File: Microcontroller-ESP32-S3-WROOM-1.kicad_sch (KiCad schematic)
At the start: 17 parts, among them U1 ESP32-S3-WROOM-1, U4 CP2102N-Axx-xQFN20

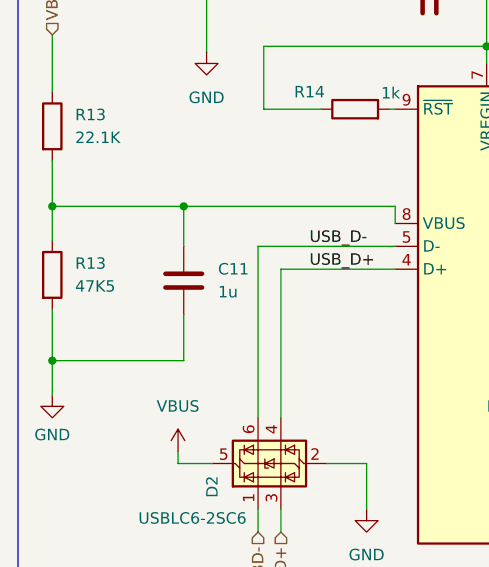
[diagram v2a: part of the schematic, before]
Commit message: refactor(schematic): update resistor footprints and component metadata
Change resistor footprints from 0805 to 0201 metric and populate detailed component properties including manufacturer, part numbers, datasheets, and distributor links for improved BOM accuracy.
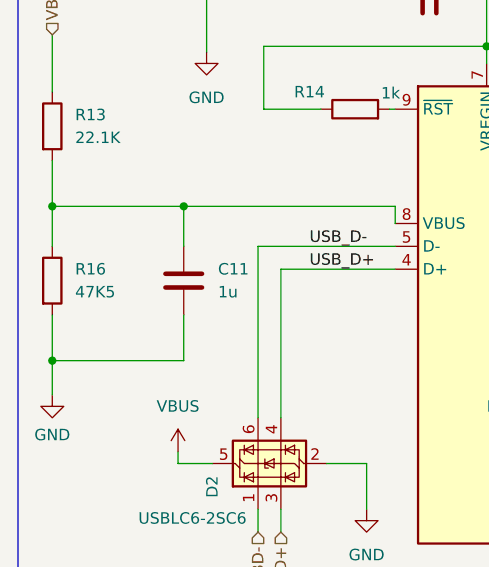
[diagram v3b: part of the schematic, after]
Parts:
- removed R13: 47K5, Resistor_SMD:R_0805_2012Metric, symbol Device:R
- added R16: 47K5, Resistor_SMD:R_0201_0603Metric, symbol Device:R
- R13: footprint Resistor_SMD:R_0805_2012Metric -> Resistor_SMD:R_0201_0603Metric; Distributor_link_1 (none) -> https://eu.mouser.com/ProductDetail/Susumu/RG0603Q-2212-D-T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; Distributor_link_2 (none) -> https://www.digikey.com/en/products/detail/susumu/RG0603Q-2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; LCSC (none) -> https://www.lcsc.com/search?q=VES4R7M1VTR-0405&s_z=n_q_VES4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; Manufacturer (none) -> Susumu; Manufacturer_part_number (none) -> RG0603Q-2212-D-T10
- R14: footprint Resistor_SMD:R_0805_2012Metric -> Resistor_SMD:R_0201_0603Metric; Distributor_link_1 (none) -> https://eu.mouser.com/ProductDetail/Susumu/RG0603P-102-B-T1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; Distributor_link_2 (none) -> https://www.digikey.com/en/products/detail/susumu/RG0603P-1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; LCSC (none) -> C20135023; Manufacturer (none) -> Susumu; Manufacturer_part_number (none) -> RG0603P-102-B-T10
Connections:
- net GND: now also R16.2
- net at C11.1, R13.2, U4.8 (VBUS): now also R16.1
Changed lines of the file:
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@@
-	(wire
-		(pts
-			(xy 19.05 153.035) (xy 19.05 158.75)
-		)
-		(stroke
-			(width 0)
-			(type default)
-		)
-	)
 	(wire
 		(pts
@@
 	(wire
 		(pts
+			(xy 19.05 141.605) (xy 19.05 146.05)
+		)
+		(stroke
+			(width 0)
+			(type default)
+		)
+	)
+	(wire
+		(pts
 			(xy 57.15 141.605) (xy 57.15 143.51)
 		)
@@
 	(wire
 		(pts
+			(xy 19.05 153.67) (xy 19.05 158.75)
+		)
+		(stroke
+			(width 0)
+			(type default)
+		)
+	)
+	(wire
+		(pts
 			(xy 82.55 168.91) (xy 86.36 168.91)
 		)
@@
 		(pts
 			(xy 44.45 165.1) (xy 44.45 148.59)
-		)
-		(stroke
-			(width 0)
-			(type default)
-		)
-	)
-	(wire
-		(pts
-			(xy 19.05 141.605) (xy 19.05 145.415)
 		)
 		(stroke
@@
 			)
 		)
-		(property "Footprint" "Resistor_SMD:R_0805_2012Metric"
+		(property "Footprint" "Resistor_SMD:R_0201_0603Metric"
 			(at 17.272 132.715 90)
 			(effects
@@
 			)
 		)
-		(property "Datasheet" "~"
+		(property "Datasheet" "https://eu.mouser.com/datasheet/3/826/1/n_catalog_partition01_en.pdf"
 			(at 19.05 132.715 0)
 			(effects
@@
 			)
 		)
-		(property "Description" "Resistor"
+		(property "Description" "Thin Film Resistors - SMD Thin Film Chip Resistors 0201 size, 0.063W, 22.1K ohm, 0.5%, 50ppm AEC Q200 Qualified Anti-sulfur"
+			(at 19.05 132.715 0)
+			(effects
+				(font
+					(size 1.27 1.27)
+				)
+				(hide yes)
+			)
+		)
+		(property "Manufacturer" "Susumu"
+			(at 19.05 132.715 0)
+			(effects
+				(font
+					(size 1.27 1.27)
+				)
+				(hide yes)
+			)
+		)
+		(property "Manufacturer_part_number" "RG0603Q-2212-D-T10"
+			(at 19.05 132.715 0)
+			(effects
+				(font
+					(size 1.27 1.27)
+				)
+				(hide yes)
+			)
+		)
+		(property "Distributor_link_1" "https://eu.mouser.com/ProductDetail/Susumu/RG0603Q-2212-D-T10?qs=amGC7iS6iy8tfDEqHW4FPw%3D%3D"
+			(at 19.05 132.715 0)
+			(effects
+				(font
+					(size 1.27 1.27)
+				)
+				(hide yes)
+			)
+		)
+		(property "Distributor_link_2" "https://www.digikey.com/en/products/detail/susumu/RG0603Q-2212-D-T10/18103229?s=N4IgTCBcDaIEoHEAMA2JBmAigWjGAjGNgCLYAq%2BSIAugL5A"
+			(at 19.05 132.715 0)
+			(effects
+				(font
+					(size 1.27 1.27)
+				)
+				(hide yes)
+			)
+		)
+		(property "LCSC" "https://www.lcsc.com/search?q=VES4R7M1VTR-0405&s_z=n_q_VES4R7M1VTR-0405"
 			(at 19.05 132.715 0)
 			(effects
@@
 			)
 		)
-		(property "Footprint" "Resistor_SMD:R_0805_2012Metric"
+		(property "Footprint" "Resistor_SMD:R_0201_0603Metric"
 			(at 52.705 132.588 90)
 			(effects
@@
 			)
 		)
-		(property "Datasheet" "~"
+		(property "Datasheet" "https://eu.mouser.com/datasheet/3/826/1/n_catalog_partition01_en.pdf"
 			(at 52.705 130.81 0)
 			(effects
@@
 			)
 		)
-		(property "Description" "Resistor"
+		(property "Description" "Thin Film Resistors - SMD Thin Film Chip Resistors 0201 size, 0.063W, 1K ohm, 0.1%, 25ppm AEC Q200 Qualified Anti-sulfur"
 			(at 52.705 130.81 0)
+			(effects
+				(font
+					(size 1.27 1.27)
+				)
+				(hide yes)
+			)
+		)
+		(property "Manufacturer" "Susumu"
+			(at 52.705 130.81 90)
+			(effects
+				(font
+					(size 1.27 1.27)
+				)
+				(hide yes)
+			)
+		)
+		(property "Manufacturer_part_number" "RG0603P-102-B-T10"
+			(at 52.705 130.81 90)
+			(effects
+				(font
+					(size 1.27 1.27)
+				)
+				(hide yes)
+			)
+		)
+		(property "Distributor_link_1" "https://eu.mouser.com/ProductDetail/Susumu/RG0603P-102-B-T10?qs=amGC7iS6iy%2F0QPamw0jmkg%3D%3D"
+			(at 52.705 130.81 90)
+			(effects
+				(font
+					(size 1.27 1.27)
+				)
+				(hide yes)
+			)
+		)
+		(property "Distributor_link_2" "https://www.digikey.com/en/products/detail/susumu/RG0603P-102-B-T10/18103206?s=N4IgTCBcDaIEoHEAMA2JBmACgWgIxLGwCFsAVfEAXQF8g"
+			(at 52.705 130.81 90)
+			(effects
+				(font
+					(size 1.27 1.27)
+				)
+				(hide yes)
+			)
+		)
+		(property "LCSC" "C20135023"
+			(at 52.705 130.81 90)
 			(effects
 				(font
@@
 	)
 	(symbol
+		(lib_id "Device:R")
+		(at 19.05 149.86 0)
+		(unit 1)
+		(exclude_from_sim no)
+		(in_bom yes)
+		(on_board yes)
+		(dnp no)
+		(fields_autoplaced yes)
+		(property "Reference" "R16"
+			(at 21.59 148.5899 0)
+			(effects
+				(font
+					(size 1.27 1.27)
+				)
+				(justify left)
+			)
+		)
+		(property "Value" "47K5"
+			(at 21.59 151.1299 0)
+			(effects
+				(font
+					(size 1.27 1.27)
+				)
+				(justify left)
+			)
+		)
+		(property "Footprint" "Resistor_SMD:R_0201_0603Metric"
+			(at 17.272 149.86 90)
+			(effects
+				(font
+					(size 1.27 1.27)
+				)
+				(hide yes)
+			)
+		)
+		(property "Datasheet" "https://eu.mouser.com/datasheet/3/826/1/n_catalog_partition01_en.pdf"
+			(at 19.05 149.86 0)
+			(effects
+				(font
+					(size 1.27 1.27)
+				)
+				(hide yes)
+			)
+		)
+		(property "Description" "Thin Film Resistors - SMD Thin Film Chip Resistors 0201 size, 0.063W, 47.5K ohm, 0.5%, 50ppm AEC Q200 Qualified Anti-sulfur"
+			(at 19.05 149.86 0)
+			(effects
+				(font
+					(size 1.27 1.27)
+				)
+				(hide yes)
+			)
+		)
+		(property "Manufacturer" "Susumu"
+			(at 19.05 149.86 0)
+			(effects
+				(font
+					(size 1.27 1.27)
+				)
+				(hide yes)
+			)
+		)
+		(property "Manufacturer_part_number" "RG0603Q-2212-D-T10"
+			(at 19.05 149.86 0)
+			(effects
+				(font
+					(size 1.27 1.27)
+				)
+				(hide yes)
+			)
+		)
+		(property "Distributor_link_1" "https://eu.mouser.com/ProductDetail/Susumu/RG0603Q-2212-D-T10?qs=amGC7iS6iy8tfDEqHW4FPw%3D%3D"
+			(at 19.05 149.86 0)
+			(effects
+				(font
+					(size 1.27 1.27)
+				)
+				(hide yes)
+			)
+		)
+		(property "Distributor_link_2" "https://www.digikey.com/en/products/detail/susumu/RG0603Q-2212-D-T10/18103229?s=N4IgTCBcDaIEoHEAMA2JBmAigWjGAjGNgCLYAq%2BSIAugL5A"
+			(at 19.05 149.86 0)
+			(effects
+				(font
+					(size 1.27 1.27)
+				)
+				(hide yes)
+			)
+		)
+		(property "LCSC" "https://www.lcsc.com/search?q=VES4R7M1VTR-0405&s_z=n_q_VES4R7M1VTR-0405"
+			(at 19.05 149.86 0)
+			(effects
+				(font
+					(size 1.27 1.27)
+				)
+				(hide yes)
+			)
+		)
+		(pin "2"
+		)
+		(pin "1"
+		)
+		(instances
+			(project "iot_device_pcb"
+				(path "/20a6db8f-6f9d-426b-a90e-3cd30ac36ee8/d76e5a61-e019-4441-8e0f-87cbb4ce42a5"
+					(reference "R16")
+					(unit 1)
+				)
+			)
+		)
+	)
+	(symbol
 		(lib_id "Interface_USB:CP2102N-Axx-xQFN20")
 		(at 69.85 153.67 0)
@@
 					(unit 1)
 				)
-			)
-		)
-	)
-	(symbol
-		(lib_id "Device:R")
-		(at 19.05 149.225 0)
-		(unit 1)
-		(exclude_from_sim no)
-		(in_bom yes)
-		(on_board yes)
-		(dnp no)
-		(fields_autoplaced yes)
-		(property "Reference" "R13"
-			(at 21.59 147.9549 0)
-			(effects
-				(font
-					(size 1.27 1.27)
-				)
-				(justify left)
-			)
-		)
-		(property "Value" "47K5"
-			(at 21.59 150.4949 0)
-			(effects
-				(font
-					(size 1.27 1.27)
-				)
-				(justify left)
-			)
-		)
-		(property "Footprint" "Resistor_SMD:R_0805_2012Metric"
-			(at 17.272 149.225 90)
-			(effects
-				(font
-					(size 1.27 1.27)
-				)
-				(hide yes)
-			)
-		)
-		(property "Datasheet" "~"
-			(at 19.05 149.225 0)
-			(effects
-				(font
-					(size 1.27 1.27)
-				)
-				(hide yes)
-			)
-		)
-		(property "Description" "Resistor"
-			(at 19.05 149.225 0)
-			(effects
-				(font
-					(size 1.27 1.27)
-				)
-				(hide yes)
-			)
-		)
-		(pin "2"
-		)
-		(pin "1"
-		)
-		(instances
-			(project "iot_device_pcb"
-				(path "/20a6db8f-6f9d-426b-a90e-3cd30ac36ee8/d76e5a61-e019-4441-8e0f-87cbb4ce42a5"
-					(reference "R13")
-					(unit 1)
-				)

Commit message: fix(schematic): correct component part numbers and LCSC identifiers
Update manufacturer part numbers and LCSC part codes to ensure correct component selection and procurement accuracy.
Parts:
- R13: LCSC https://www.lcsc.com/search?q=VES4R7M1VTR-0405&s_z=n_q_VES4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 -> C20136319
- R16: Distributor_link_1 https://eu.mouser.com/ProductDetail/Susumu/RG0603Q-2212-D-T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 -> https://eu.mouser.com/ProductDetail/Susumu/RG0603Q-4752-D-T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; Distributor_link_2 https://www.digikey.com/en/products/detail/susumu/RG0603Q-2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 -> https://www.digikey.com/en/products/detail/susumu/RG0603Q-4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; LCSC https://www.lcsc.com/search?q=VES4R7M1VTR-0405&s_z=n_q_VES4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 -> C20136872; Manufacturer_part_number RG0603Q-2212-D-T10 -> RG0603Q-4752-D-T10
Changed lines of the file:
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@@
 			)
 		)
-		(property "LCSC" "https://www.lcsc.com/search?q=VES4R7M1VTR-0405&s_z=n_q_VES4R7M1VTR-0405"
+		(property "LCSC" "C20136319"
 			(at 19.05 132.715 0)
 			(effects
@@
 			)
 		)
-		(property "Manufacturer_part_number" "RG0603Q-2212-D-T10"
-			(at 19.05 149.86 0)
-			(effects
-				(font
-					(size 1.27 1.27)
-				)
-				(hide yes)
-			)
-		)
-		(property "Distributor_link_1" "https://eu.mouser.com/ProductDetail/Susumu/RG0603Q-2212-D-T10?qs=amGC7iS6iy8tfDEqHW4FPw%3D%3D"
-			(at 19.05 149.86 0)
-			(effects
-				(font
-					(size 1.27 1.27)
-				)
-				(hide yes)
-			)
-		)
-		(property "Distributor_link_2" "https://www.digikey.com/en/products/detail/susumu/RG0603Q-2212-D-T10/18103229?s=N4IgTCBcDaIEoHEAMA2JBmAigWjGAjGNgCLYAq%2BSIAugL5A"
-			(at 19.05 149.86 0)
-			(effects
-				(font
-					(size 1.27 1.27)
-				)
-				(hide yes)
-			)
-		)
-		(property "LCSC" "https://www.lcsc.com/search?q=VES4R7M1VTR-0405&s_z=n_q_VES4R7M1VTR-0405"
-			(at 19.05 149.86 0)
-			(effects
+		(property "Manufacturer_part_number" "RG0603Q-4752-D-T10"
+			(at 19.05 149.86 0)
+			(effects
+				(font
+					(size 1.27 1.27)
+				)
+				(hide yes)
+			)
+		)
+		(property "Distributor_link_1" "https://eu.mouser.com/ProductDetail/Susumu/RG0603Q-4752-D-T10?qs=amGC7iS6iy%2FSgGA%2FUnp6Ag%3D%3D"
+			(at 19.05 149.86 0)
+			(effects
+				(font
+					(size 1.27 1.27)
+				)
+				(hide yes)
+			)
+		)
+		(property "Distributor_link_2" "https://www.digikey.com/en/products/detail/susumu/RG0603Q-4752-D-T10/18103021?s=N4IgTCBcDaIEoHEAMA2JBmAigWgCwHYBWMbAEWwBUBGJEAXQF8g"
+			(at 19.05 149.86 0)
+			(effects
+				(font
+					(size 1.27 1.27)
+				)
+				(hide yes)
+			)
+		)
+		(property "LCSC" "C20136872"
+			(at 19.05 149.86 0)
+			(effects

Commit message: fix(schematic): replace power symbol with BC817 transistor
Replaces the redundant +3.3V power symbol with a BC817 NPN transistor component, including proper footprint (SOT-23), datasheet link, and pin definitions.
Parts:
- added C12: 1u, Capacitor_SMD:C_0805_2012Metric, symbol Device:C
- added C13: 0.1u, Capacitor_SMD:C_0805_2012Metric, symbol Device:C
- added Q1, Q2: BC817, Package_TO_SOT_SMD:SOT-23, symbol Transistor_BJT:BC817
- added R17, R18, R19: 10K, Resistor_SMD:R_0805_2012Metric, symbol Device:R
- added S1, S2: USLPT2819DT2TR, FootPrints:SW_USLPT2819DT2TR, symbol USLPT2819DT2TR:USLPT2819DT2TR
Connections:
- net +3.3V: now also R19.1
- net EN: now also C12.1, Q2.3 (C), R19.2, S2.3, S2.4
- net GND: now also C12.2, C13.2, S1.1, S1.2, S2.1, S2.2
- net RTS: now also Q2.2 (E), R17.2
- net RX_TX: now also U1.37 (TXD0)
- net TX_RX: now also U1.36 (RXD0)
- net BOOT: now reaches U1.27 (IO0)
- net BOOT: now also C13.1, Q1.2 (E), S1.3, S1.4
- new net: Q1.1 (B), R17.1
- new net: Q2.1 (B), R18.1
- new net DTR: Q1.3 (C), R18.2
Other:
- added sheet Actuators (Actuators.kicad_sch)
- added sheet Display (Display.kicad_sch)
- added sheet Sensors (Sensors.kicad_sch)
- note added: "AUTO Program DTR RTS -> EN I00 I02 1 1 1 1 1 0 0 1 1 1 1 0 0 1 1 0 1 1 0 0"
- note added: "BOOT"
- note added: "BOOT/EN"
- note added: "RESET"
- moved on the sheet: C5, C7, C8, C9
